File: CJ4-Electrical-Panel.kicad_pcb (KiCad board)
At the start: 2 copper layers, 122.4 x 62.5 mm, 42 parts, among them J1 Conn_01x03, J2 Conn_01x03, J3 Conn_01x03, J4 Conn_01x03, J5 Conn_01x03, J6 Conn_01x03, J8 AVR-ISP-6, U1 ATmega32U4-A, Y1 16MHz

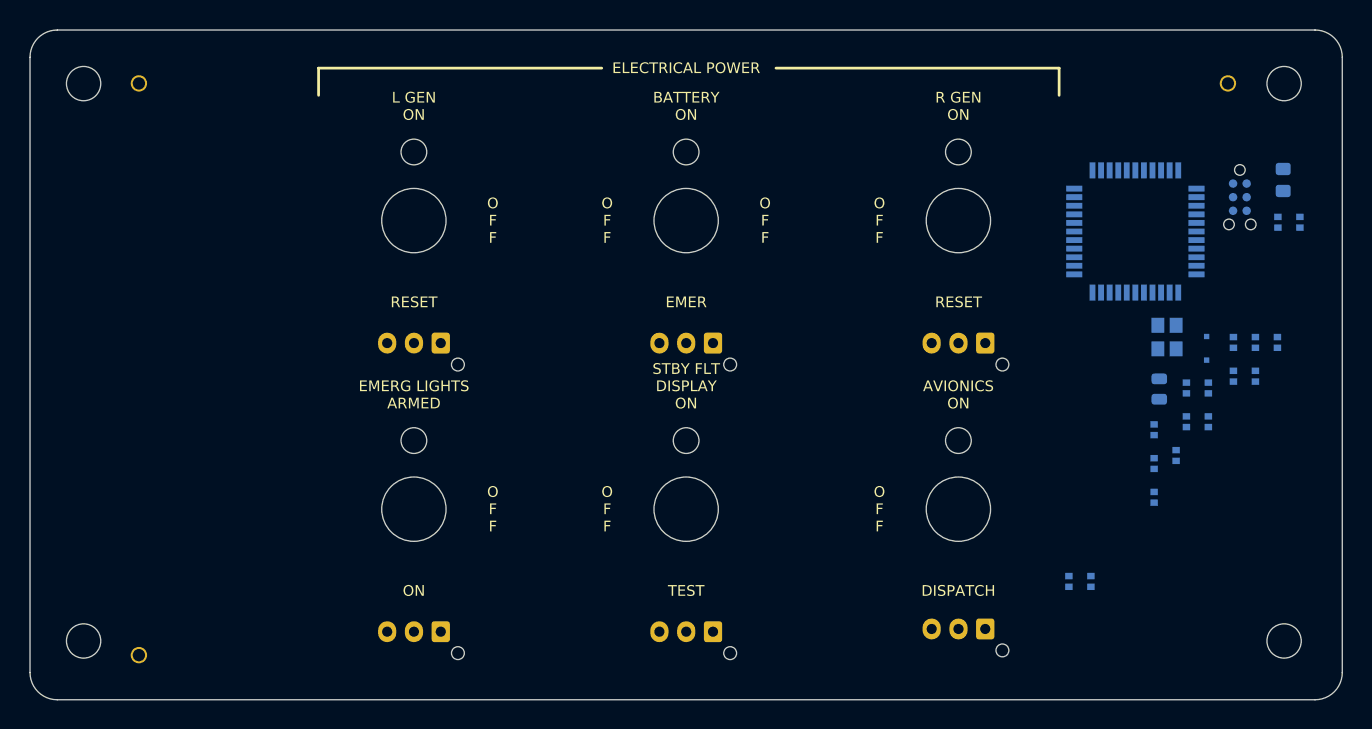
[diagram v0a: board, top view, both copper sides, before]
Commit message: Finish routing, add JLCPCB part numbers
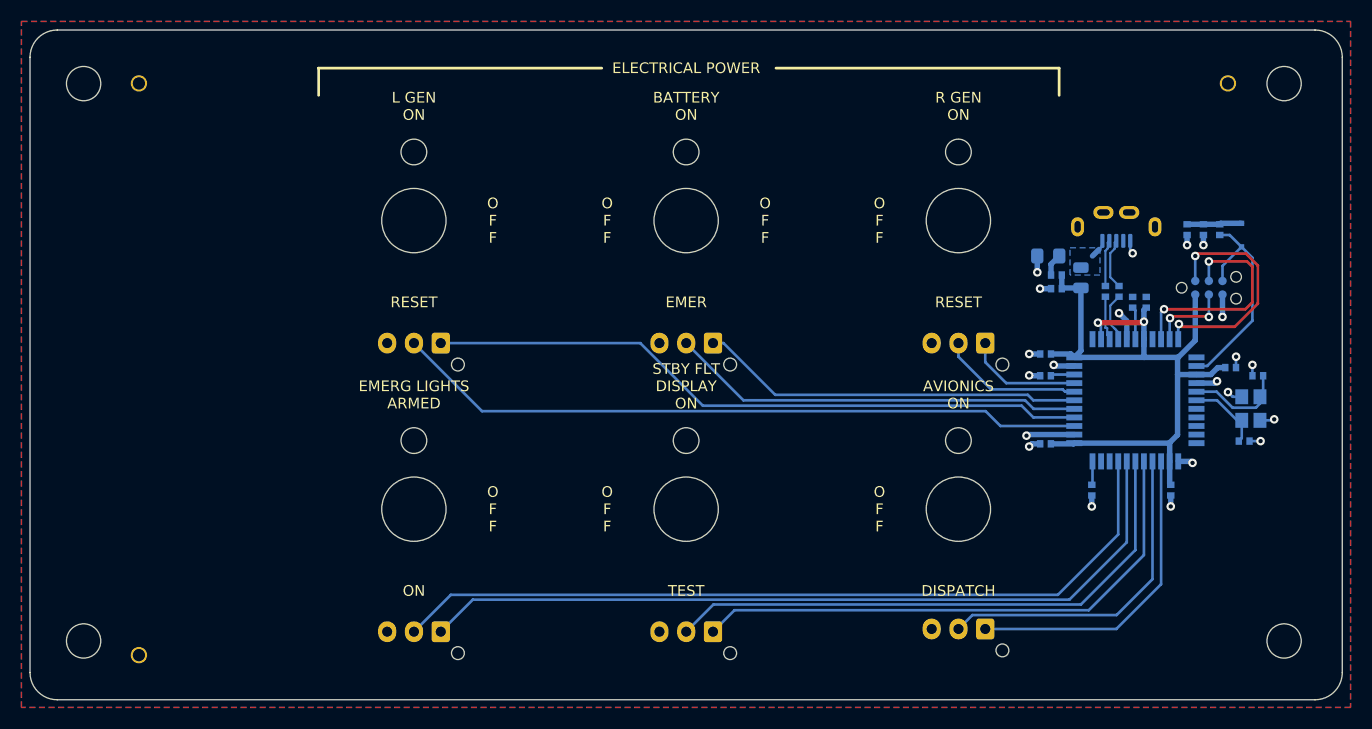
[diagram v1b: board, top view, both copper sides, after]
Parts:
- added J7: USB_B_Mini, CJ4-Electrical-Panel:ZX80-B-5P, B.Cu at (152.1, 69.1)
- moved C3 26.3 mm to (153.7, 76.2), turned to 90 degrees
- moved C1 26.0 mm to (145.5, 83.1), turned to 180 degrees
- moved C12 25.2 mm to (158.8, 69.4)
- moved D2 23.0 mm to (145.8, 71.9), turned to 0 degrees
- moved R5 22.7 mm to (161.8, 69.4)
- moved C10 21.2 mm to (146.6, 74.9), turned to 180 degrees
- moved R4 19.7 mm to (146.6, 73.7), turned to 180 degrees
- moved C8 18.6 mm to (145.5, 89.4), turned to 180 degrees
- moved R2 18.1 mm to (152.4, 75.2)
- moved C4 15.9 mm to (157.2, 93.7)
- moved U1 15.7 mm to (153.9, 85.3)
- moved C11 14.8 mm to (160.3, 69.4)
- moved C2 14.6 mm to (154.9, 76.2), turned to 90 degrees
- moved FB1 12.7 mm to (148.8, 73.9)
- moved C9 12.3 mm to (145.6, 81.0), turned to 180 degrees
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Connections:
- FB1 pad 1: Net-(FB1-Pad1) -> /VBUS
- R2 pad 1: Net-(J7-Pad3) -> /DR+
- R3 pad 1: Net-(J7-Pad2) -> /DR-
- U1 pad 10: BATTERY_ON -> /MOSI
- U1 pad 11: BATTERY_EMER -> /MISO
- U1 pad 12: EMERLT_ON -> unconnected-(U1-Pad12)
- U1 pad 18: AVIONICS_ON -> unconnected-(U1-Pad18)
- U1 pad 19: AVIONICS_DISPATCH -> unconnected-(U1-Pad19)
- U1 pad 25: unconnected-(U1-Pad25) -> AVIONICS_ON
- U1 pad 26: unconnected-(U1-Pad26) -> AVIONICS_DISPATCH
- U1 pad 27: unconnected-(U1-Pad27) -> RGEN_ON
- U1 pad 28: RGEN_ON -> RGEN_RESET
- U1 pad 29: RGEN_RESET -> STBY_ON
- U1 pad 30: EMERLT_ARMED -> STBY_TEST
- U1 pad 31: STBY_ON -> unconnected-(U1-Pad31)
- U1 pad 32: STBY_TEST -> unconnected-(U1-Pad32)
- U1 pad 36: unconnected-(U1-Pad36) -> LGEN_RESET
- U1 pad 37: unconnected-(U1-Pad37) -> LGEN_ON
- U1 pad 38: unconnected-(U1-Pad38) -> EMERLT_ON
- U1 pad 39: unconnected-(U1-Pad39) -> EMERLT_ARMED
- U1 pad 40: unconnected-(U1-Pad40) -> BATTERY_EMER
- U1 pad 41: unconnected-(U1-Pad41) -> BATTERY_ON
- U1 pad 8: LGEN_ON -> unconnected-(U1-Pad8)
- U1 pad 9: LGEN_RESET -> /SCK
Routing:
- net STBY_TEST: track 0.00 -> 76.3 mm
- net STBY_ON: track 0.00 -> 75.0 mm
- net +5V: track 0.00 -> 72.3 mm, vias 0 -> 2
- net LGEN_RESET: track 0.00 -> 64.8 mm
- net LGEN_ON: track 0.00 -> 62.0 mm
- net RGEN_RESET: track 0.00 -> 53.3 mm
- net RGEN_ON: track 0.00 -> 51.9 mm
- net EMERLT_ON: track 0.00 -> 38.7 mm
- net EMERLT_ARMED: track 0.00 -> 35.9 mm
- net GND: track 0.00 -> 31.5 mm, vias 0 -> 21
- net AVIONICS_DISPATCH: track 0.00 -> 31.0 mm
- net AVIONICS_ON: track 0.00 -> 29.6 mm
- net /MISO: track 0.00 -> 22.1 mm, vias 0 -> 2
- net /SCK: track 0.00 -> 20.8 mm, vias 0 -> 2
- net RESET: track 0.00 -> 20.7 mm
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- added copper zone on B.Cu, net /VBUS
- added copper zone on B.Cu, net GND
- added copper zone on F.Cu, net GND

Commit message: Update to KiCad v6 automation
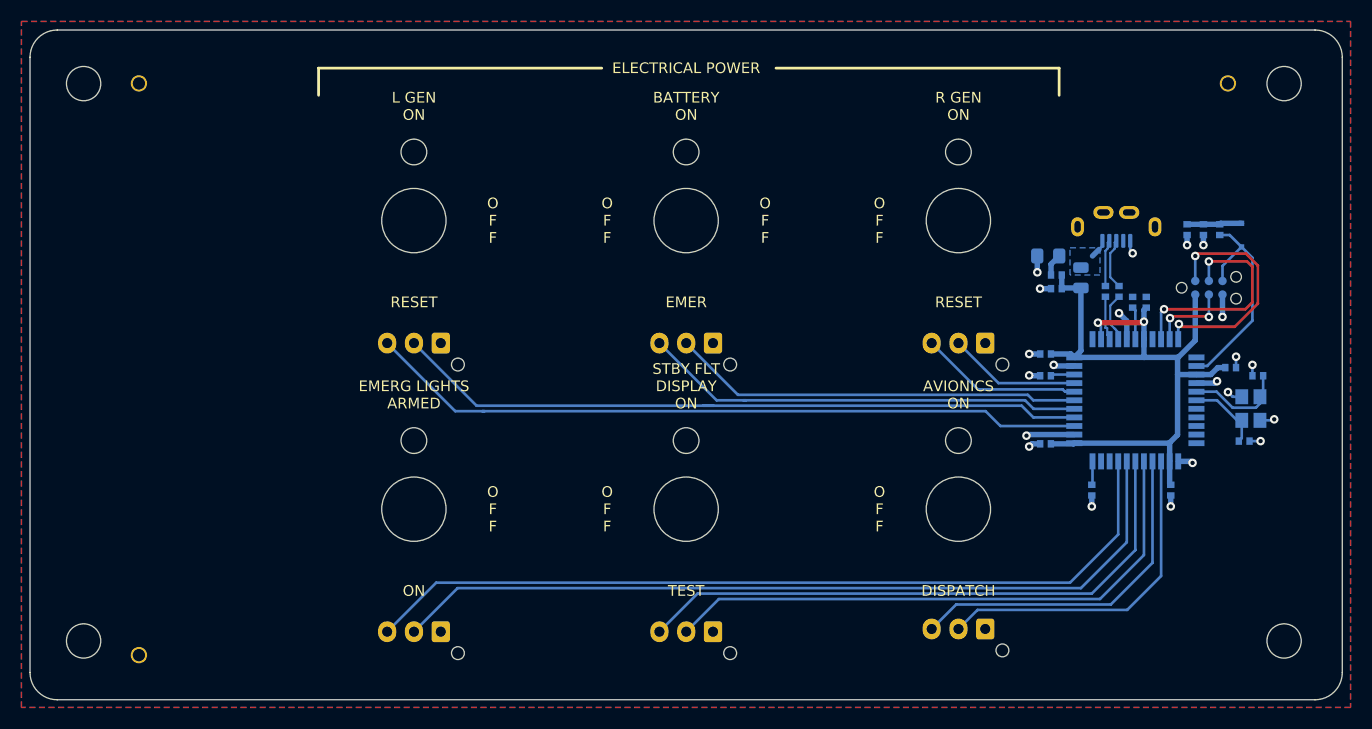
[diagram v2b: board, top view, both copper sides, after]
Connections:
- J1 pad 1: LGEN_ON -> GND
- J1 pad 2: LGEN_RESET -> LGEN_ON
- J1 pad 3: GND -> LGEN_RESET
- J2 pad 1: EMERLT_ARMED -> GND
- J2 pad 2: EMERLT_ON -> EMERLT_ARMED
- J2 pad 3: GND -> EMERLT_ON
- J3 pad 1: BATTERY_ON -> GND
- J3 pad 2: BATTERY_EMER -> BATTERY_ON
- J3 pad 3: GND -> BATTERY_EMER
- J4 pad 1: STBY_ON -> GND
- J4 pad 2: STBY_TEST -> STBY_ON
- J4 pad 3: GND -> STBY_TEST
- J5 pad 1: RGEN_ON -> GND
- J5 pad 2: RGEN_RESET -> RGEN_ON
- J5 pad 3: GND -> RGEN_RESET
- J6 pad 1: AVIONICS_ON -> GND
- J6 pad 2: AVIONICS_DISPATCH -> AVIONICS_ON
- J6 pad 3: GND -> AVIONICS_DISPATCH
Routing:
- net LGEN_ON: track 62.0 -> 65.5 mm
- net LGEN_RESET: track 64.8 -> 67.6 mm
- net EMERLT_ON: track 38.7 -> 41.5 mm
- net STBY_ON: track 75.0 -> 77.5 mm
- net STBY_TEST: track 76.3 -> 78.8 mm
- net RGEN_RESET: track 53.3 -> 55.8 mm
- net RGEN_ON: track 51.9 -> 54.4 mm
- net EMERLT_ARMED: track 35.9 -> 38.4 mm
- net AVIONICS_ON: track 29.6 -> 31.6 mm
- net BATTERY_EMER: track 13.4 -> 15.2 mm
- net AVIONICS_DISPATCH: track 31.0 -> 32.6 mm
- net BATTERY_ON: track 10.9 -> 12.3 mm
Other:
- board text added: "JLCJLCJLCJLC"

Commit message: Add date and version placeholders
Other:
- board text added: "CJ4 electrical panel Neil Enns neile@live.com @date@ @version@ JLCJLCJLCJLC"
- board text removed: "JLCJLCJLCJLC"
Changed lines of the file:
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@@
   (paper "A4")
   (title_block
-    (rev "")
+    (title "CJ4 electrical panel")
+    (rev "@version@")
+    (comment 1 "Neil Enns")
+    (comment 2 "neile@live.com")
   )
   (layers
@@
   (gr_arc (start 173.228 110.744) (mid 172.484051 112.540051) (end 170.688 113.284) (layer "Edge.Cuts") (width 0.1))
   (gr_arc (start 53.34 113.284) (mid 51.543949 112.540051) (end 50.8 110.744) (layer "Edge.Cuts") (width 0.1))
-  (gr_text "JLCJLCJLCJLC" (at 153.162 108.966) (layer "B.SilkS")
+  (gr_text "CJ4 electrical panel\nNeil Enns neile@live.com\n@date@\n@version@\nJLCJLCJLCJLC" (at 67.564 101.854) (layer "B.SilkS")
     (effects (font (size 1 1) (thickness 0.15)) (justify mirror))
   )
